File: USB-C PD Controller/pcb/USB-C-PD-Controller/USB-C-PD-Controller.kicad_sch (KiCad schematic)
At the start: 2 parts, among them J1 Conn_02x04_Odd_Even, J2 Conn_02x04_Odd_Even

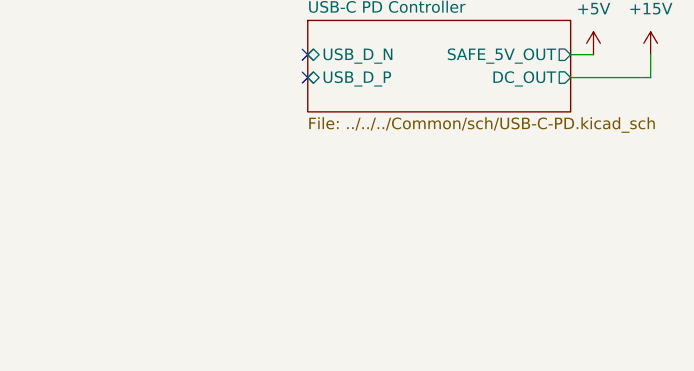
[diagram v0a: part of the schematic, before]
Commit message: USB-C PD Controller finishing touches
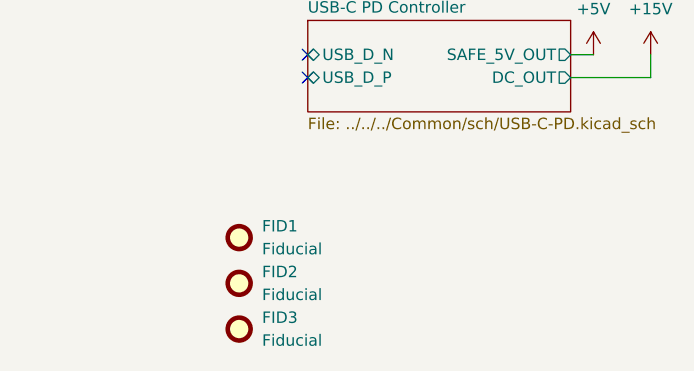
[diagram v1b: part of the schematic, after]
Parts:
- added FID1, FID2, FID3: Fiducial, Fiducial:Fiducial_1mm_Mask2mm, symbol Mechanical:Fiducial
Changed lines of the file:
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@@
 (kicad_sch
-	(version 20231120)
+	(version 20250114)
 	(generator "eeschema")
-	(generator_version "8.0")
+	(generator_version "9.0")
 	(paper "A4")
 	(junction
@@
 	)
 	(symbol
+		(lib_id "Mechanical:Fiducial")
+		(at 81.28 139.7 0)
+		(unit 1)
+		(exclude_from_sim yes)
+		(in_bom no)
+		(on_board yes)
+		(dnp no)
+		(fields_autoplaced yes)
+		(property "Reference" "FID3"
+			(at 83.82 138.4299 0)
+			(effects
+				(font
+					(size 1.27 1.27)
+				)
+				(justify left)
+			)
+		)
+		(property "Value" "Fiducial"
+			(at 83.82 140.9699 0)
+			(effects
+				(font
+					(size 1.27 1.27)
+				)
+				(justify left)
+			)
+		)
+		(property "Footprint" "Fiducial:Fiducial_1mm_Mask2mm"
+			(at 81.28 139.7 0)
+			(effects
+				(font
+					(size 1.27 1.27)
+				)
+				(hide yes)
+			)
+		)
+		(property "Datasheet" "~"
+			(at 81.28 139.7 0)
+			(effects
+				(font
+					(size 1.27 1.27)
+				)
+				(hide yes)
+			)
+		)
+		(property "Description" "Fiducial Marker"
+			(at 81.28 139.7 0)
+			(effects
+				(font
+					(size 1.27 1.27)
+				)
+				(hide yes)
+			)
+		)
+		(property "Purchase" ""
+			(at 81.28 139.7 0)
+			(effects
+				(font
+					(size 1.27 1.27)
+				)
+				(hide yes)
+			)
+		)
+		(instances
+			(project "USB-C-PD-Controller"
+				(path "/21fe6961-ba77-4b1f-af4e-dd494ba8e8ee"
+					(reference "FID3")
+					(unit 1)
+				)
+			)
+		)
+	)
+	(symbol
+		(lib_id "Mechanical:Fiducial")
+		(at 81.28 129.54 0)
+		(unit 1)
+		(exclude_from_sim yes)
+		(in_bom no)
+		(on_board yes)
+		(dnp no)
+		(fields_autoplaced yes)
+		(property "Reference" "FID1"
+			(at 83.82 128.2699 0)
+			(effects
+				(font
+					(size 1.27 1.27)
+				)
+				(justify left)
+			)
+		)
+		(property "Value" "Fiducial"
+			(at 83.82 130.8099 0)
+			(effects
+				(font
+					(size 1.27 1.27)
+				)
+				(justify left)
+			)
+		)
+		(property "Footprint" "Fiducial:Fiducial_1mm_Mask2mm"
+			(at 81.28 129.54 0)
+			(effects
+				(font
+					(size 1.27 1.27)
+				)
+				(hide yes)
+			)
+		)
+		(property "Datasheet" "~"
+			(at 81.28 129.54 0)
+			(effects
+				(font
+					(size 1.27 1.27)
+				)
+				(hide yes)
+			)
+		)
+		(property "Description" "Fiducial Marker"
+			(at 81.28 129.54 0)
+			(effects
+				(font
+					(size 1.27 1.27)
+				)
+				(hide yes)
+			)
+		)
+		(property "Purchase" ""
+			(at 81.28 129.54 0)
+			(effects
+				(font
+					(size 1.27 1.27)
+				)
+				(hide yes)
+			)
+		)
+		(instances
+			(project "USB-C-PD-Controller"
+				(path "/21fe6961-ba77-4b1f-af4e-dd494ba8e8ee"
+					(reference "FID1")
+					(unit 1)
+				)
+			)
+		)
+	)
+	(symbol
 		(lib_id "power:+15V")
 		(at 59.69 76.2 0)
@@
 	)
 	(symbol
+		(lib_id "Mechanical:Fiducial")
+		(at 81.28 134.62 0)
+		(unit 1)
+		(exclude_from_sim yes)
+		(in_bom no)
+		(on_board yes)
+		(dnp no)
+		(fields_autoplaced yes)
+		(property "Reference" "FID2"
+			(at 83.82 133.3499 0)
+			(effects
+				(font
+					(size 1.27 1.27)
+				)
+				(justify left)
+			)
+		)
+		(property "Value" "Fiducial"
+			(at 83.82 135.8899 0)
+			(effects
+				(font
+					(size 1.27 1.27)
+				)
+				(justify left)
+			)
+		)
+		(property "Footprint" "Fiducial:Fiducial_1mm_Mask2mm"
+			(at 81.28 134.62 0)
+			(effects
+				(font
+					(size 1.27 1.27)
+				)
+				(hide yes)
+			)
+		)
+		(property "Datasheet" "~"
+			(at 81.28 134.62 0)
+			(effects
+				(font
+					(size 1.27 1.27)
+				)
+				(hide yes)
+			)
+		)
+		(property "Description" "Fiducial Marker"
+			(at 81.28 134.62 0)
+			(effects
+				(font
+					(size 1.27 1.27)
+				)
+				(hide yes)
+			)
+		)
+		(property "Purchase" ""
+			(at 81.28 134.62 0)
+			(effects
+				(font
+					(size 1.27 1.27)
+				)
+				(hide yes)
+			)
+		)
+		(instances
+			(project "USB-C-PD-Controller"
+				(path "/21fe6961-ba77-4b1f-af4e-dd494ba8e8ee"
+					(reference "FID2")
+					(unit 1)
+				)
+			)
+		)
+	)
+	(symbol
 		(lib_id "power:GNDD")
 		(at 85.09 83.82 0)
@@
 		(at 88.9 105.41)
 		(size 29.21 10.16)
+		(exclude_from_sim no)
+		(in_bom yes)
+		(on_board yes)
+		(dnp no)
 		(fields_autoplaced yes)
 		(stroke
@@
 		)
 	)
+	(embedded_fonts no)
 )

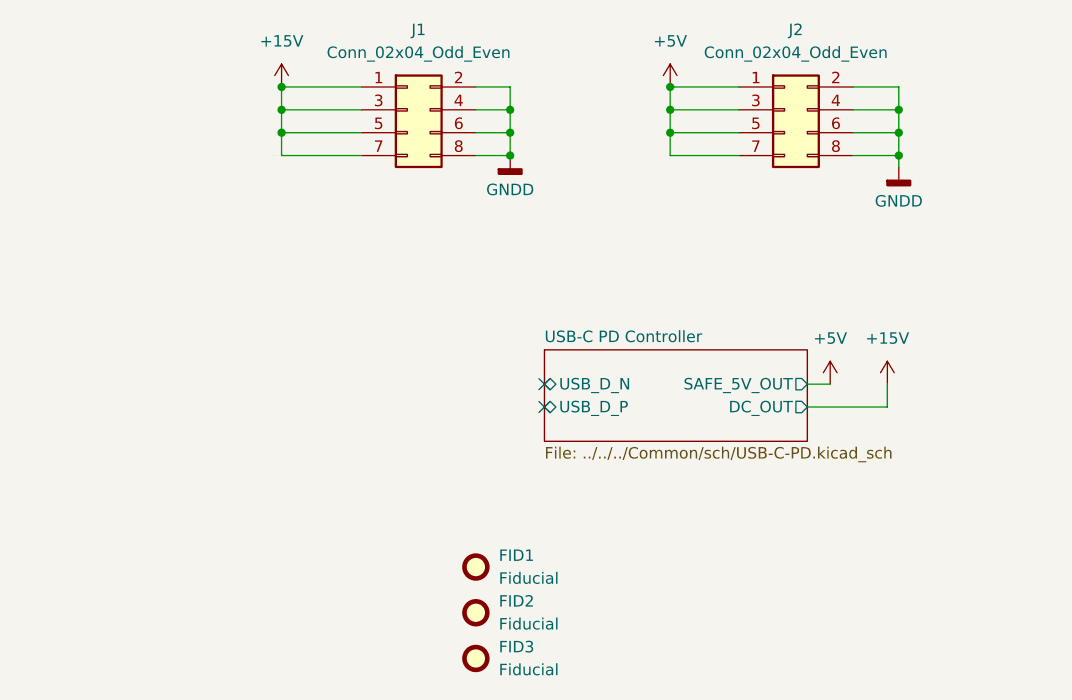
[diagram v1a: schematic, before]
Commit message: USB-C PD controller modifications because I can't make up my mind
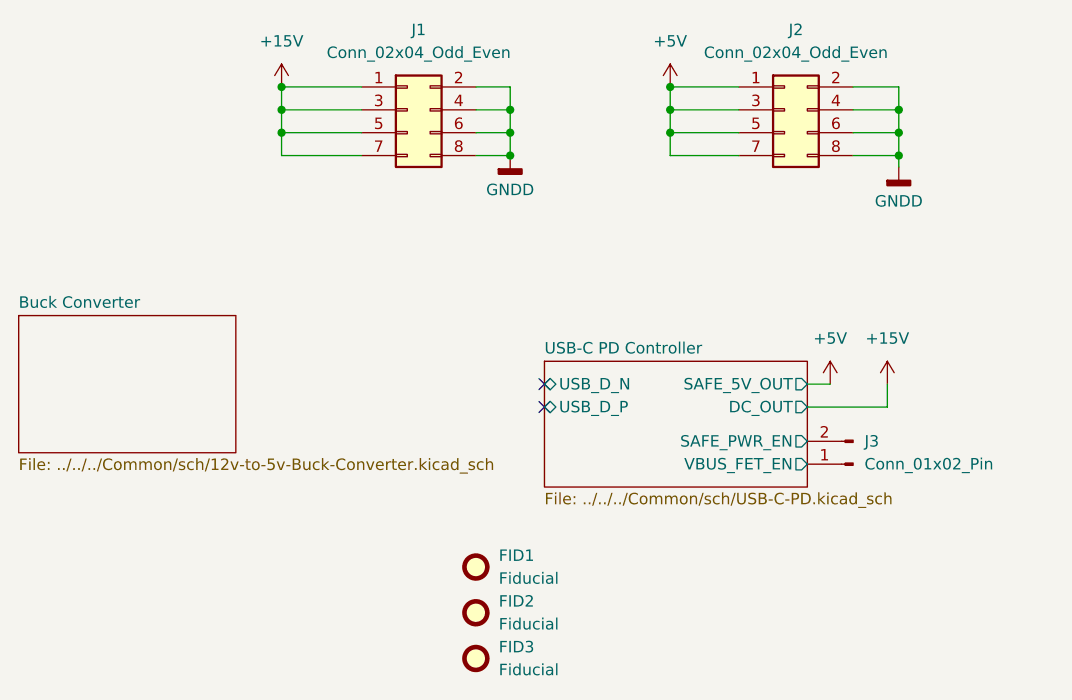
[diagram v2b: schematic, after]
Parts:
- added J3: Conn_01x02_Pin, Connector_PinHeader_2.54mm:PinHeader_1x02_P2.54mm_Vertical, symbol Connector:Conn_01x02_Pin
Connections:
- new net USB-C PD Controller/SAFE_PWR_EN: J3.2 (Pin_2)
- new net USB-C PD Controller/VBUS_FET_EN: J3.1 (Pin_1)
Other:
- added sheet Buck Converter (../../../Common/sch/12v-to-5v-Buck-Converter.kicad_sch)
- sheet USB-C PD Controller ports: added SAFE_PWR_EN, VBUS_FET_EN; removed none
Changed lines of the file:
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@@
+	)
+	(symbol
+		(lib_id "Connector:Conn_01x02_Pin")
+		(at 123.19 118.11 180)
+		(unit 1)
+		(exclude_from_sim no)
+		(in_bom yes)
+		(on_board yes)
+		(dnp no)
+		(fields_autoplaced yes)
+		(property "Reference" "J3"
+			(at 124.46 115.5699 0)
+			(effects
+				(font
+					(size 1.27 1.27)
+				)
+				(justify right)
+			)
+		)
+		(property "Value" "Conn_01x02_Pin"
+			(at 124.46 118.1099 0)
+			(effects
+				(font
+					(size 1.27 1.27)
+				)
+				(justify right)
+			)
+		)
+		(property "Footprint" "Connector_PinHeader_2.54mm:PinHeader_1x02_P2.54mm_Vertical"
+			(at 123.19 118.11 0)
+			(effects
+				(font
+					(size 1.27 1.27)
+				)
+				(hide yes)
+			)
+		)
+		(property "Datasheet" "~"
+			(at 123.19 118.11 0)
+			(effects
+				(font
+					(size 1.27 1.27)
+				)
+				(hide yes)
+			)
+		)
+		(property "Description" "Generic connector, single row, 01x02, script generated"
+			(at 123.19 118.11 0)
+			(effects
+				(font
+					(size 1.27 1.27)
+				)
+				(hide yes)
+			)
+		)
+		(pin "2"
+		)
+		(pin "1"
+		)
+		(instances
+			(project ""
+				(path "/21fe6961-ba77-4b1f-af4e-dd494ba8e8ee"
+					(reference "J3")
+					(unit 1)
+				)
+			)
+		)
 	)
 	(symbol
@@
 	)
 	(sheet
-		(at 88.9 105.41)
-		(size 29.21 10.16)
+		(at 30.48 101.6)
+		(size 24.13 15.24)
 		(exclude_from_sim no)
 		(in_bom yes)
@@
 			(color 0 0 0 0.0000)
 		)
+		(property "Sheetname" "Buck Converter"
+			(at 30.48 100.8884 0)
+			(effects
+				(font
+					(size 1.27 1.27)
+				)
+				(justify left bottom)
+			)
+		)
+		(property "Sheetfile" "../../../Common/sch/12v-to-5v-Buck-Converter.kicad_sch"
+			(at 30.48 117.4246 0)
+			(effects
+				(font
+					(size 1.27 1.27)
+				)
+				(justify left top)
+			)
+		)
+		(instances
+			(project "USB-C-PD-Controller"
+				(path "/21fe6961-ba77-4b1f-af4e-dd494ba8e8ee"
+					(page "3")
+				)
+			)
+		)
+	)
+	(sheet
+		(at 88.9 106.68)
+		(size 29.21 13.97)
+		(exclude_from_sim no)
+		(in_bom yes)
+		(on_board yes)
+		(dnp no)
+		(fields_autoplaced yes)
+		(stroke
+			(width 0.1524)
+			(type solid)
+		)
+		(fill
+			(color 0 0 0 0.0000)
+		)
 		(property "Sheetname" "USB-C PD Controller"
-			(at 88.9 104.6984 0)
+			(at 88.9 105.9684 0)
 			(effects
 				(font
@@
 		)
 		(property "Sheetfile" "../../../Common/sch/USB-C-PD.kicad_sch"
-			(at 88.9 116.1546 0)
+			(at 88.9 121.2346 0)
 			(effects
 				(font
@@
 			(effects
 				(font
+					(size 1.27 1.27)
+				)
+				(justify right)
+			)
+		)
+		(pin "VBUS_FET_EN" output
+			(at 118.11 118.11 0)
+			(effects
+				(font
+					(size 1.27 1.27)
+				)
+				(justify right)
+			)
+		)
+		(pin "SAFE_PWR_EN" output
+			(at 118.11 115.57 0)
+			(effects
+				(font
